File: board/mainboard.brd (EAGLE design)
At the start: 95 x 95 mm, 10 parts

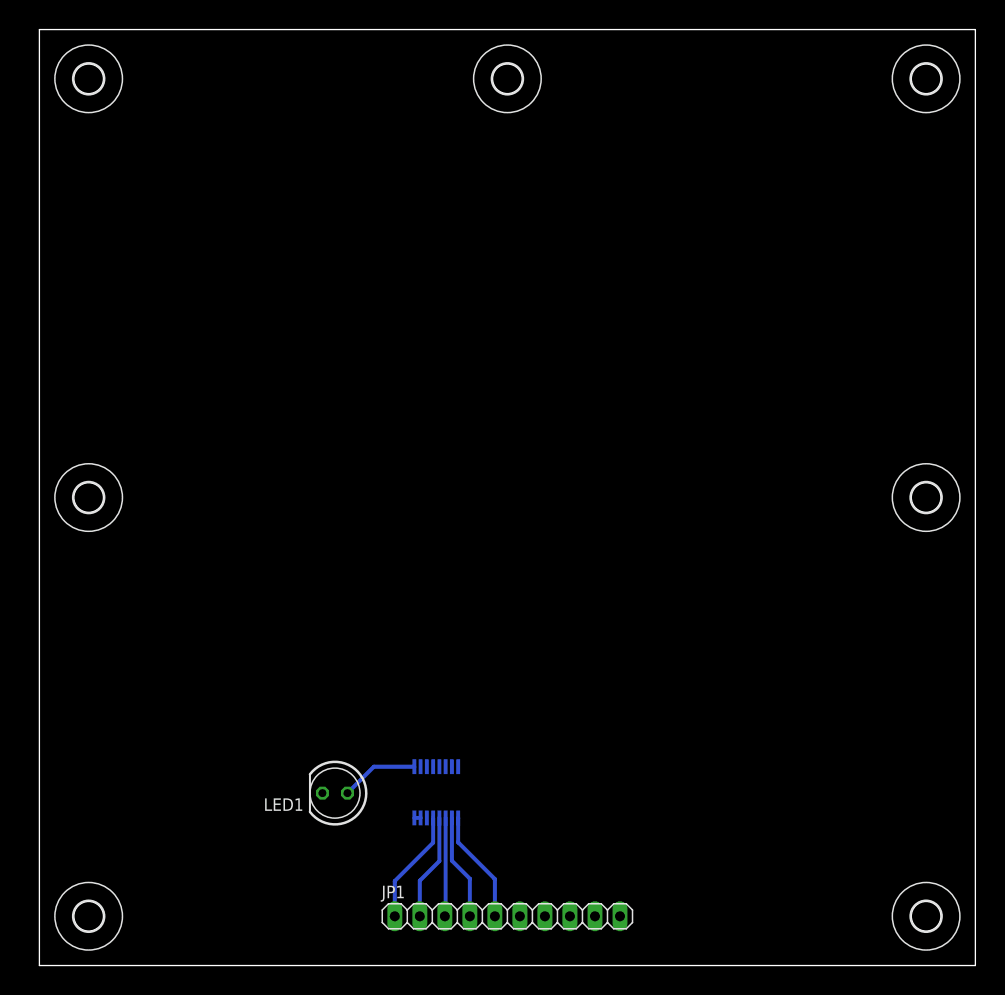
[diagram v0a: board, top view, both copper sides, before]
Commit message: board: add more components into mainboard
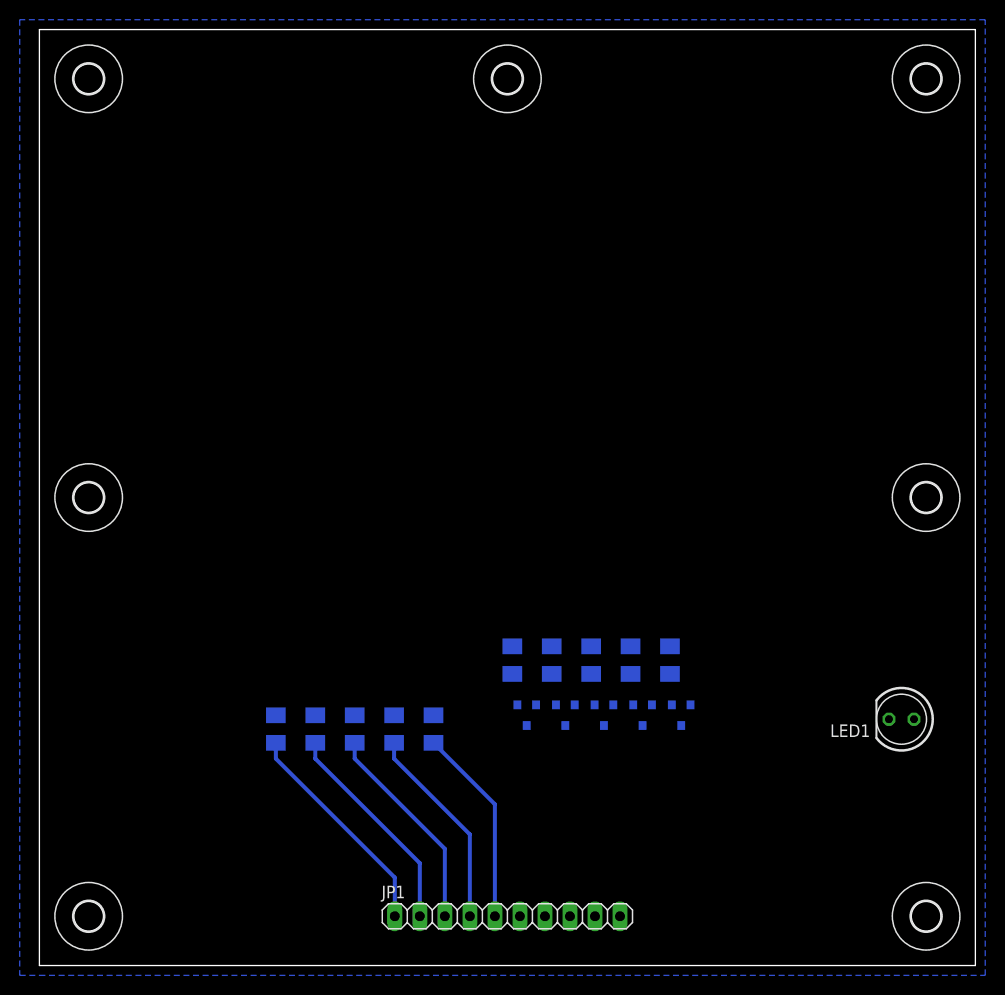
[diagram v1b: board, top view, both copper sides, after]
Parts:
- added Q1, Q2, Q3, Q4, Q5: MOSFET-NCHANNELSMD, SparkFun:SOT23-3
- added R10, R2, R3, R4, R5, R6, R7, R8, R9: (no value), rcl:M1206
- R1: value 300 -> (none); device resistor-bourns:2QSP16 -> rcl:M1206
- moved LED1 58.0 mm to (87.5, 25.0)
- moved R1 17.5 mm to (24.0, 24.0), turned to 90 degrees
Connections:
- removed net N$6: R1.7, R1.8
- removed net N$7: LED1.A, R1.9
- removed net VCC: R1.10
- new net A1: JP1.1, R1.1
- new net A2: JP1.2, R2.1
- new net A3: JP1.3, R3.1
- new net A4: JP1.4, R4.1
- new net A5: JP1.5, R5.1
- new net K1: JP1.6, Q1.3
- new net K2: JP1.7, Q2.3
- new net K3: JP1.8, Q3.3
- new net K4: JP1.9, Q4.3
- new net K5: JP1.10, Q5.3
- net GND: now also Q1.2, Q2.2, Q3.2, Q4.2, Q5.2, R10.2, R6.2, R7.2, R8.2, R9.2
- net N$1: now also Q1.1, R6.1; no longer JP1.5, R1.1
- net N$2: now also Q2.1, R7.1; no longer JP1.4, R1.2
- net N$3: now also Q3.1, R8.1; no longer JP1.3, R1.3
- net N$4: now also Q4.1, R9.1; no longer JP1.2, R1.4
- net N$5: now also Q5.1, R10.1; no longer JP1.1, R1.5
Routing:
- net A1: track 0.00 -> 22.6 mm
- net A2: track 0.00 -> 22.0 mm
- net A3: track 0.00 -> 21.4 mm
- net A4: track 0.00 -> 20.8 mm
- net A5: track 0.00 -> 20.2 mm
- net N$5: track 11.6 -> 0.00 mm
- net N$1: track 11.5 -> 0.00 mm
- net N$4: track 10.8 -> 0.00 mm
- net N$2: track 10.7 -> 0.00 mm
- net N$3: track 10.1 -> 0.00 mm
- net N$7: track 7.90 -> 0.00 mm
- net N$6: track 0.63 -> 0.00 mm
- added copper zone on layer 16, net GND

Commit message: board: add arduino to mainboard
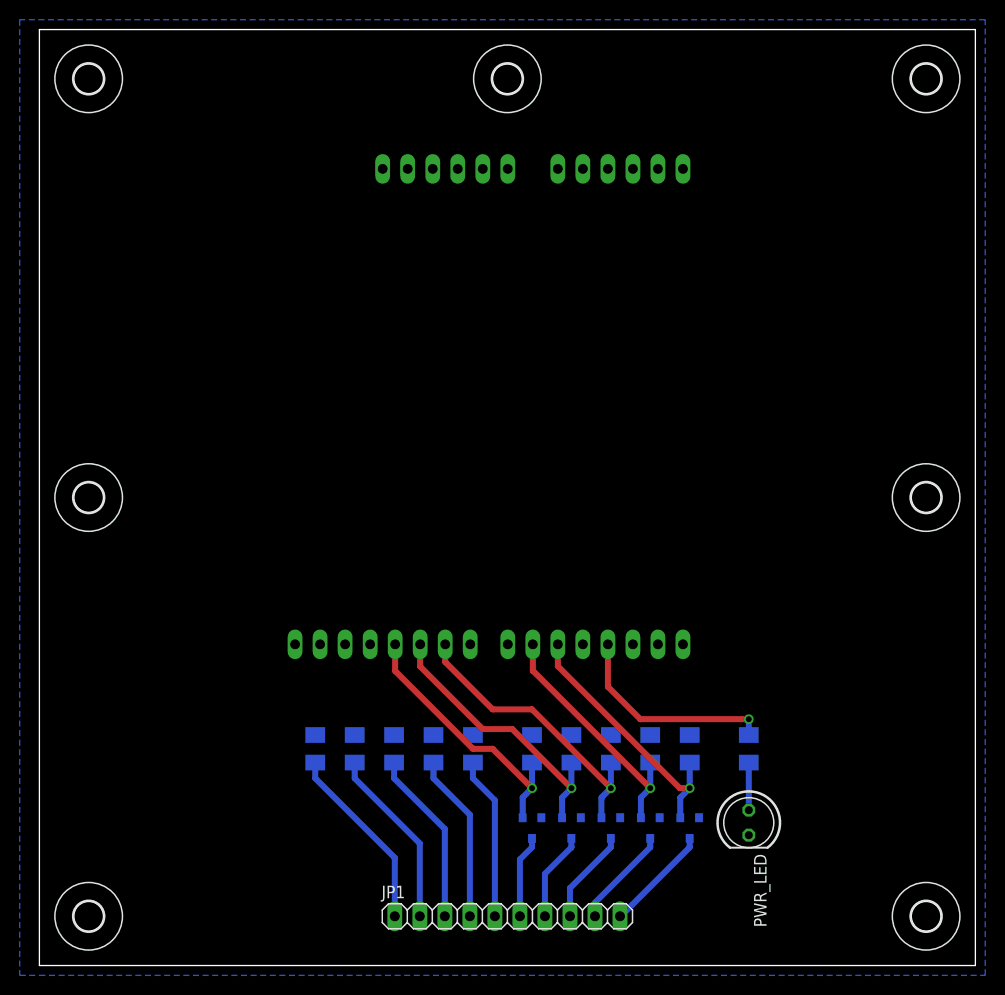
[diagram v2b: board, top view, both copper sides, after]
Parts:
- removed LED1: (no value), led:LED5MM
- added ARDUINO1: ARDUINO, arduino:ARDUINO
- added PWR_LED: (no value), led:LED5MM
- added R11: (no value), rcl:M1206
- moved Q5 11.5 mm to (66.0, 14.0)
- moved Q4 11.5 mm to (62.0, 14.0)
- moved Q3 11.5 mm to (58.0, 14.0)
- moved Q2 11.5 mm to (54.0, 14.0)
- moved Q1 11.5 mm to (50.0, 14.0)
- moved R10 9.22 mm to (66.0, 22.0)
- moved R6 9.22 mm to (50.0, 22.0)
- moved R7 9.22 mm to (54.0, 22.0)
- moved R8 9.22 mm to (58.0, 22.0)
- moved R9 9.22 mm to (62.0, 22.0)
- moved R1 4.47 mm to (28.0, 22.0)
- moved R2 4.47 mm to (32.0, 22.0)
- moved R3 4.47 mm to (36.0, 22.0)
- moved R4 4.47 mm to (40.0, 22.0)
- moved R5 4.47 mm to (44.0, 22.0)
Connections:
- removed net N$2: Q2.1, R7.1
- removed net N$3: Q3.1, R8.1
- removed net N$4: Q4.1, R9.1
- removed net N$5: Q5.1, R10.1
- new net 3V3: ARDUINO1.3V3
- new net 5V: ARDUINO1.5V
- new net COL1: ARDUINO1.12, R1.2
- new net COL2: ARDUINO1.08, R2.2
- new net COL3: ARDUINO1.07, R3.2
- new net COL4: ARDUINO1.04, R4.2
- new net COL5: ARDUINO1.02, R5.2
- new net GND1: ARDUINO1.GND2
- new net GND2: ARDUINO1.GND3
- new net LED_SEC: ARDUINO1.03, R11.2
- new net ROW1: ARDUINO1.11, Q1.1, R6.1
- new net ROW2: ARDUINO1.10, Q2.1, R7.1
- new net ROW3: ARDUINO1.09, Q3.1, R8.1
- new net ROW4: ARDUINO1.06, Q4.1, R9.1
- new net ROW5: ARDUINO1.05, Q5.1, R10.1
- new net VIN: ARDUINO1.VIN
- net GND: now also ARDUINO1.GND, PWR_LED.K; no longer LED1.K
- net N$1: now also PWR_LED.A, R11.1; no longer Q1.1, R6.1
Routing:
- net ROW3: track 0.00 -> 29.9 mm, vias 0 -> 1
- net ROW2: track 0.00 -> 28.7 mm, vias 0 -> 1
- net ROW1: track 0.00 -> 27.5 mm, vias 0 -> 1
- net ROW5: track 0.00 -> 26.7 mm, vias 0 -> 1
- net ROW4: track 0.00 -> 25.5 mm, vias 0 -> 1
- net LED_SEC: track 0.00 -> 21.6 mm, vias 0 -> 1
- net K5: track 0.00 -> 10.9 mm
- net K4: track 0.00 -> 10.2 mm
- net K3: track 0.00 -> 9.62 mm
- net K2: track 0.00 -> 9.01 mm
- net K1: track 0.00 -> 8.41 mm
- net N$1: track 0.00 -> 4.83 mm
- net A5: track 20.2 -> 16.5 mm
- net A3: track 21.4 -> 17.7 mm
- net A4: track 20.8 -> 17.1 mm
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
